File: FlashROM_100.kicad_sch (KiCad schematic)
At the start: 6 parts

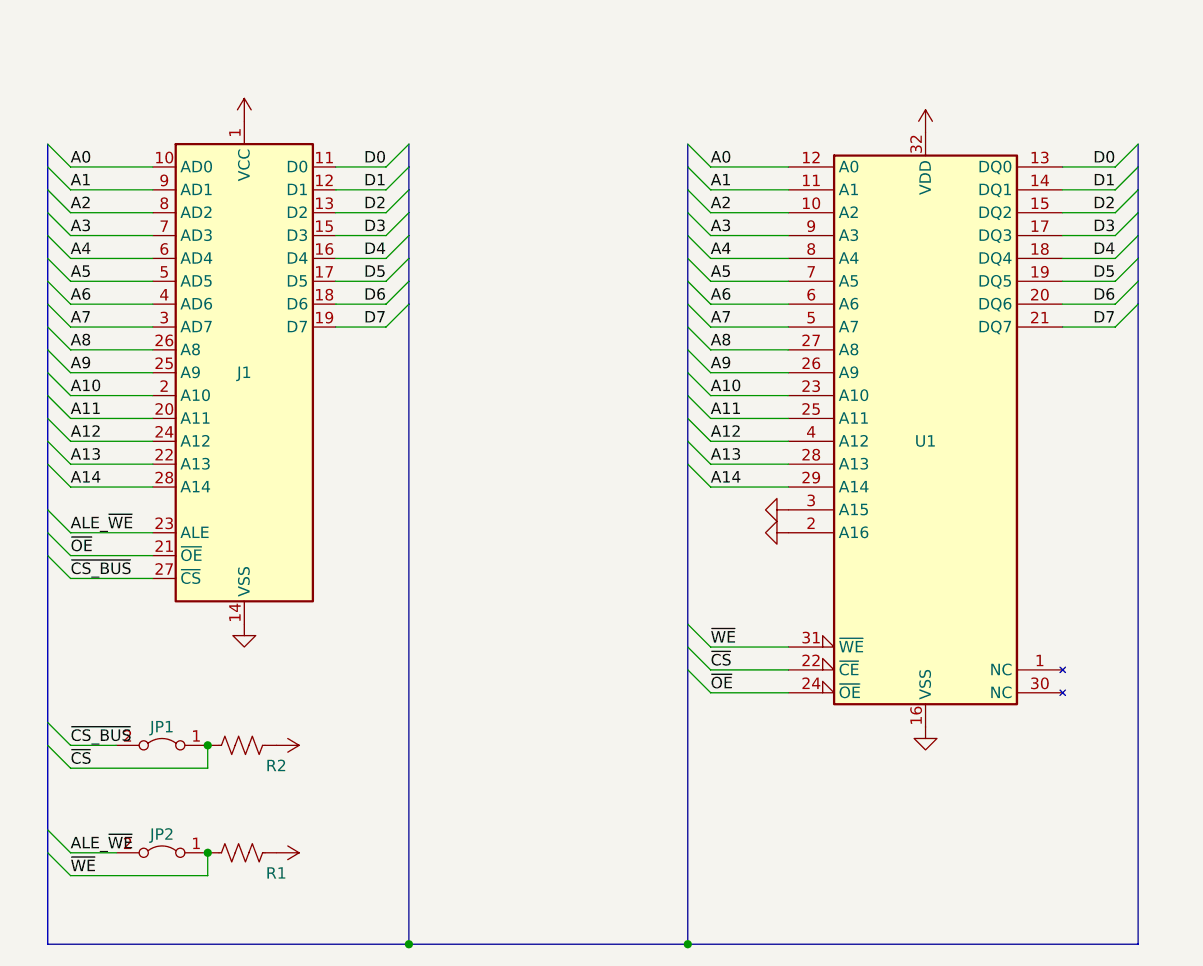
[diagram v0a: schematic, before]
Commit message: Fix wrong pinout on FlashROM_100 TSOPgit add -A!
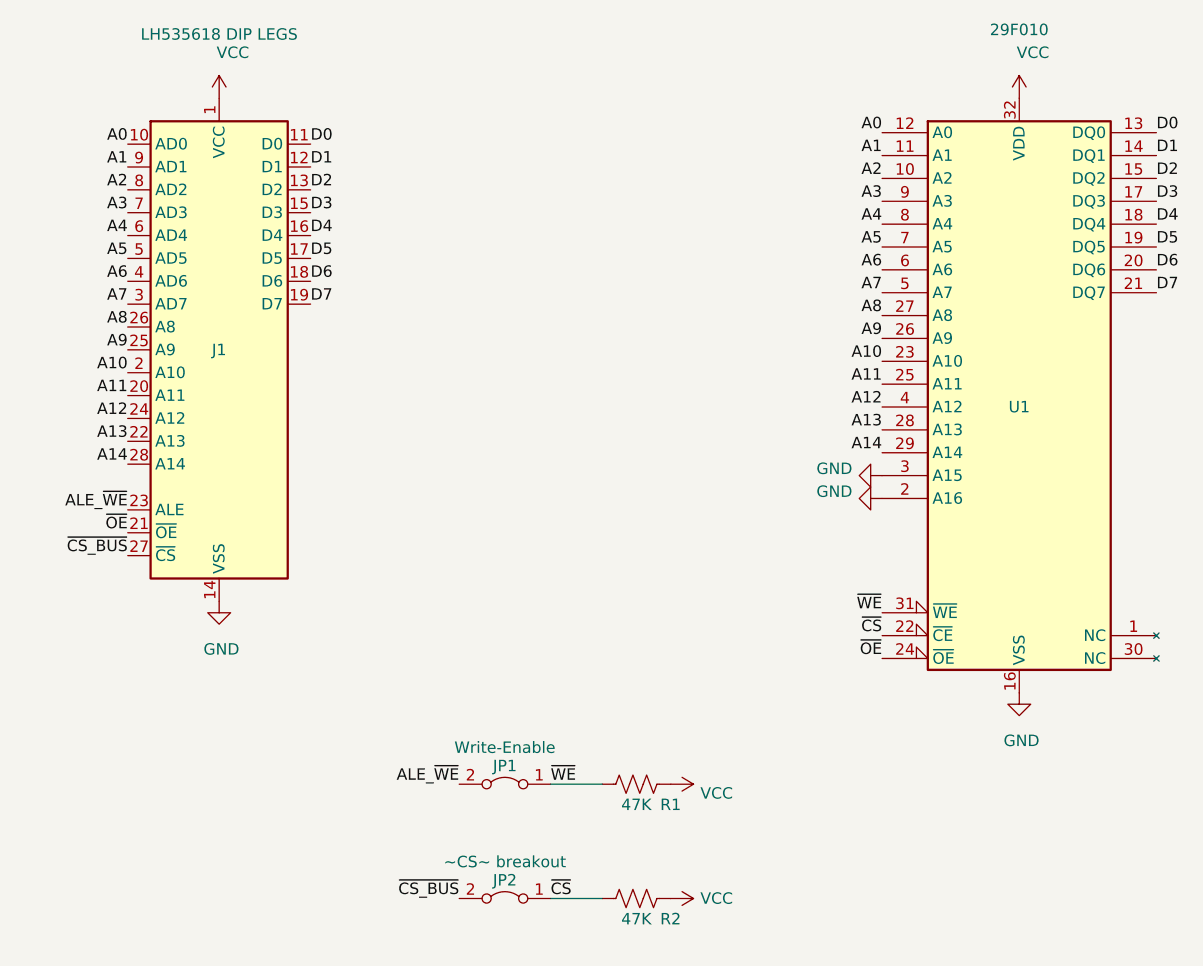
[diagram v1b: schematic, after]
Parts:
- J1: value (none) -> LH535618 DIP LEGS; footprint (none) -> 000_LOCAL:DIP28_0.6_pcb
- JP1: renamed from JP2; value (none) -> Write-Enable; footprint (none) -> 000_LOCAL:Pin_Header_Angled_1x02_Pitch2.54mm
- JP2: renamed from JP1; value (none) -> ~CS~ breakout; footprint (none) -> 000_LOCAL:Pin_Header_Angled_1x02_Pitch2.54mm
- R1, R2: value (none) -> 47K; footprint (none) -> 000_LOCAL:R_0805
- U1: value (none) -> 29F010; footprint (none) -> 000_LOCAL:PLCC32_7x9
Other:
- moved on the sheet: J1, JP1, JP2, R1, R2, U1
